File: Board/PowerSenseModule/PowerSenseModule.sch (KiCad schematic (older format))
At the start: 12 parts

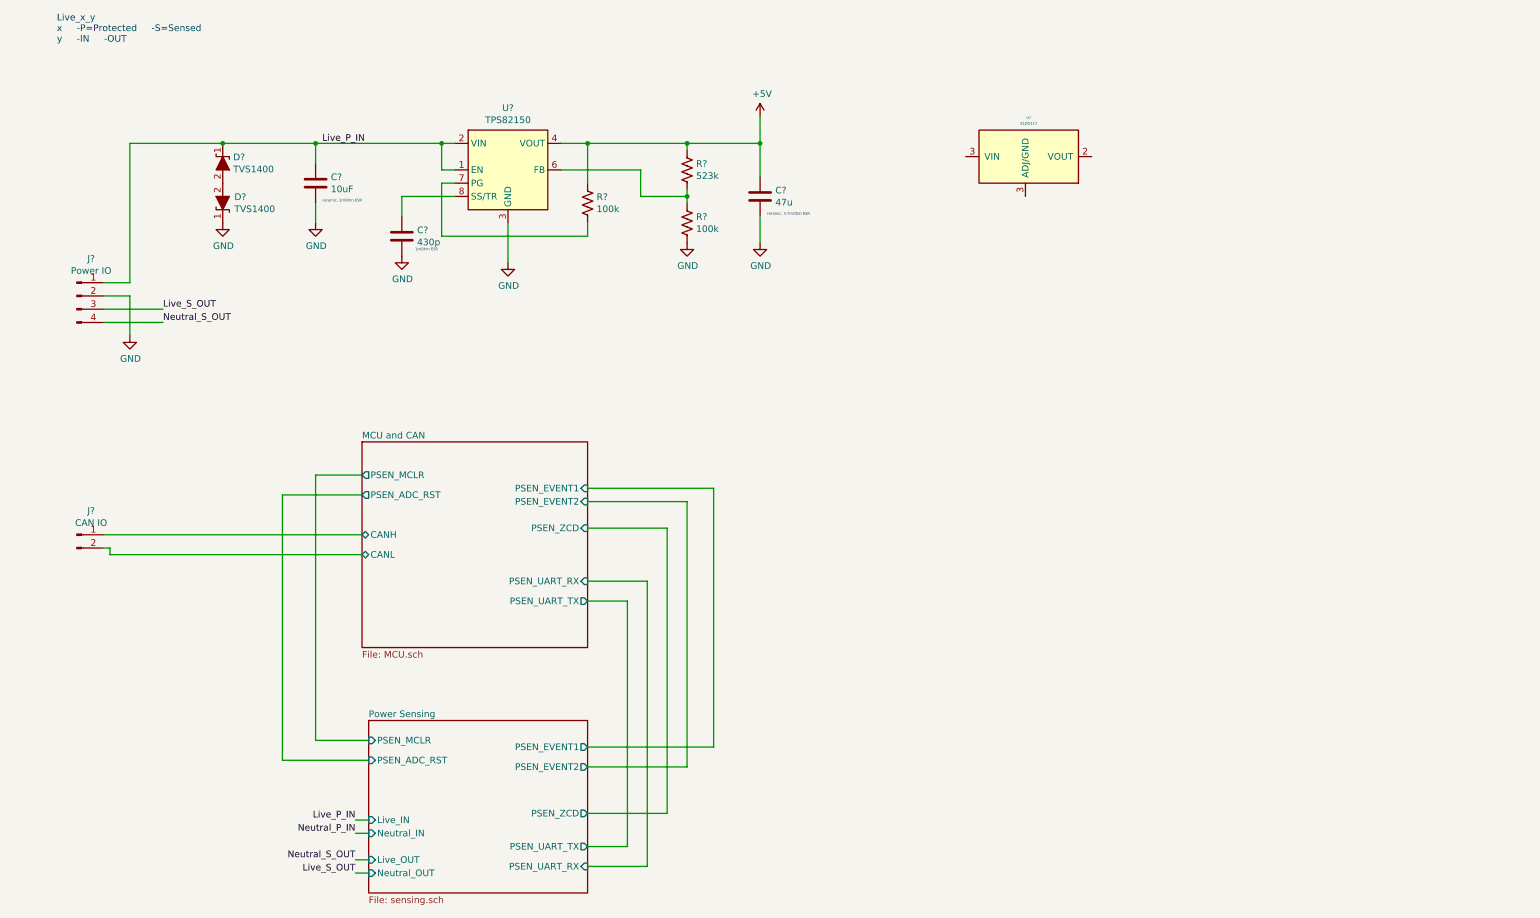
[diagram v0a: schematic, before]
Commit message: Added linear reg, cleaned up schematic
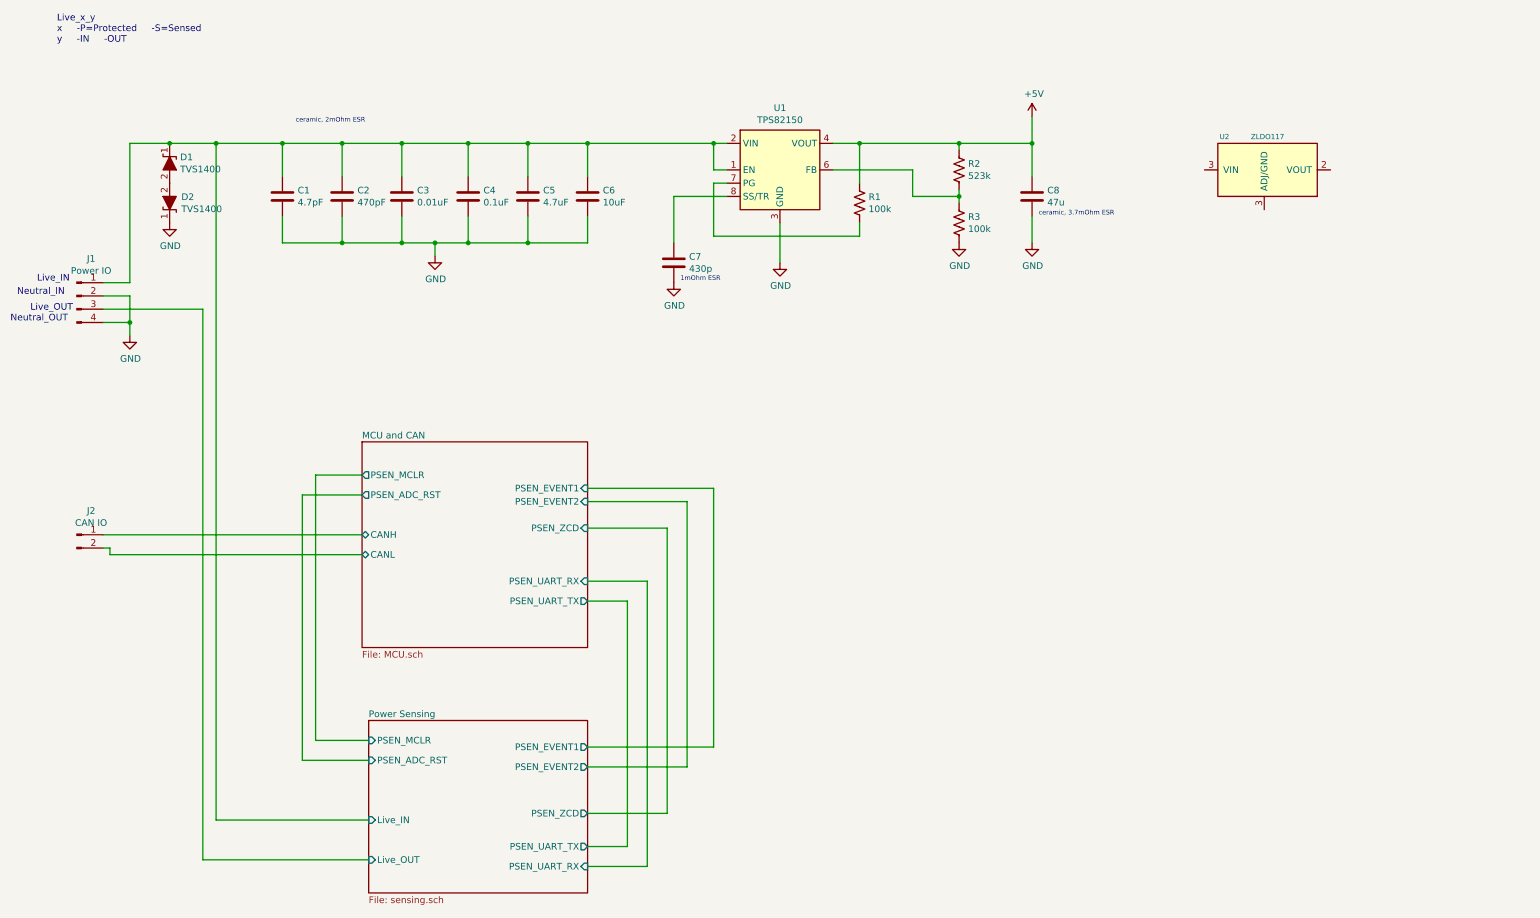
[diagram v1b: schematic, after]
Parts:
- added C1: 4.7pF, symbol Device:C
- added C2: 470pF, symbol Device:C
- added C3: 0.01uF, symbol Device:C
- added C4: 0.1uF, symbol Device:C
- added C5: 4.7uF, symbol Device:C
- gave numbers to parts that had none: 12
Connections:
- net Neutral_S_OUT is gone; now on net GND: J1.4 (Pin_4)
- net GND: now also C1.2, C2.2, C3.2, C4.2, C5.2
- net Live_P_IN renamed Power Sensing/Live_IN
- net Power Sensing/Live_IN: now also C1.1, C2.1, C3.1, C4.1, C5.1
- net Live_S_OUT renamed Power Sensing/Live_OUT
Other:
- note added: "Live_IN\n"
- note added: "Live_OUT\n\n"
- note added: "Neutral_IN\n"
- note added: "Neutral_OUT"
- moved on the sheet: C6, C7, C8, D1, D2, R1, R2, R3, U1, U2

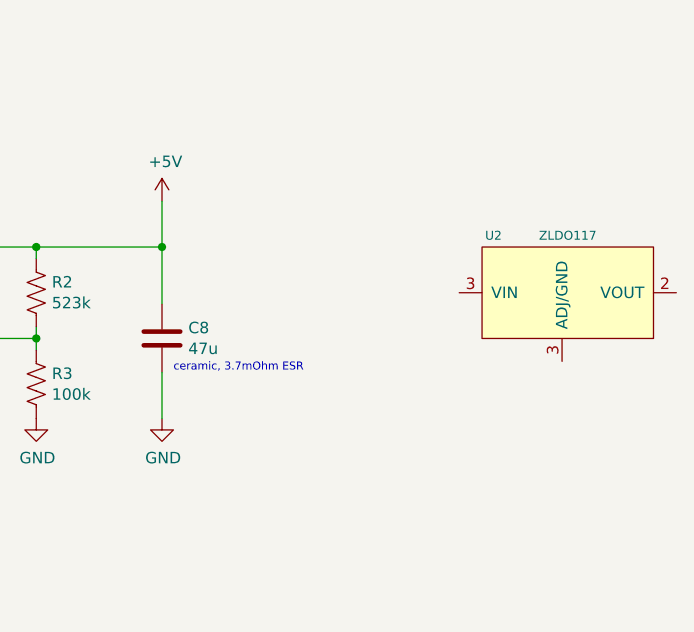
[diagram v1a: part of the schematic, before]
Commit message: Lin Reg Connected with cap, global power net, and wiring.
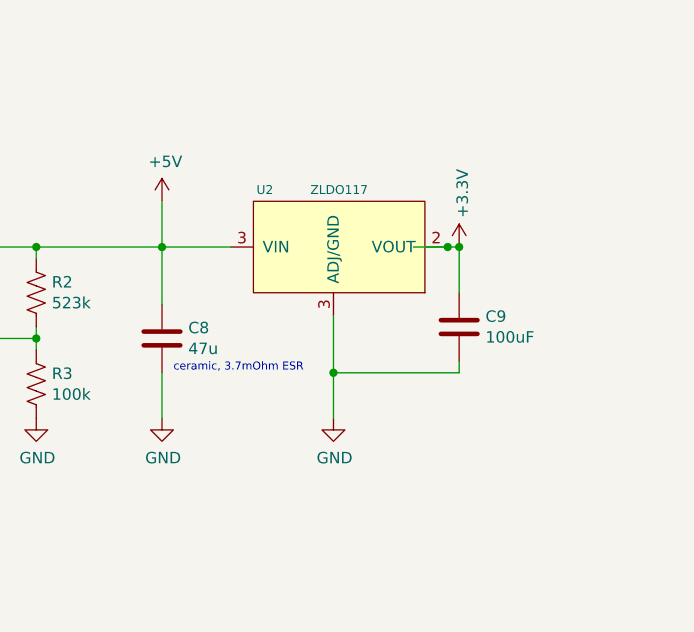
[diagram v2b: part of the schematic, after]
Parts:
- added C9: 100uF, symbol Device:C
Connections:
- net +5V: now also U2.3 (VIN)
- net GND: now also U2.3 (VIN), C9.2
- net +3V3: now reaches U2.2 (VOUT)
- net +3V3: now also C9.1
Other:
- moved on the sheet: U2
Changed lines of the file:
@@
 L F1_Power_ICs:ZLDO117 U2
 U 1 1 5D37AF29
-P 9950 1750
-F 0 "U2" H 9650 2000 39  0000 C CNN
-F 1 "ZLDO117" H 9975 2000 39  0000 C CNN
-F 2 "Package_TO_SOT_SMD:SOT-223" H 9800 2100 20  0001 C CNN
-F 3 "https://www.diodes.com/assets/Datasheets/ZLDO1117Q.pdf" H 9800 2100 20  0001 C CNN
-	1    9950 1750
+P 8950 1550
+F 0 "U2" H 8650 1800 39  0000 C CNN
+F 1 "ZLDO117" H 8975 1800 39  0000 C CNN
+F 2 "Package_TO_SOT_SMD:SOT-223" H 8800 1900 20  0001 C CNN
+F 3 "https://www.diodes.com/assets/Datasheets/ZLDO1117Q.pdf" H 8800 1900 20  0001 C CNN
+	1    8950 1550
 	1    0    0    -1
 $EndComp
@@
 Text Notes 500  2900 0    50   ~ 0
 Neutral_OUT
+$Comp
+L power:GND #PWR?
+U 1 1 5D33134A
+P 8950 2300
+F 0 "#PWR?" H 8950 2050 50  0001 C CNN
+F 1 "GND" H 8955 2127 50  0000 C CNN
+F 2 "" H 8950 2300 50  0001 C CNN
+F 3 "" H 8950 2300 50  0001 C CNN
+	1    8950 2300
+	1    0    0    -1
+$EndComp
+Wire Wire Line
+	8950 1850 8950 2100
+Wire Wire Line
+	8500 1550 8200 1550
+Wire Wire Line
+	9450 1550 9500 1550
+Connection ~ 8950 2100
+Wire Wire Line
+	8950 2100 8950 2300
+Wire Wire Line
+	9500 2100 8950 2100
+Connection ~ 9500 1550
+Wire Wire Line
+	9300 1550 9450 1550
+$Comp
+L Device:C C9
+U 1 1 5D39E84F
+P 9500 1900
+F 0 "C9" H 9615 1946 50  0000 L CNN
+F 1 "100uF" H 9615 1855 50  0000 L CNN
+F 2 "" H 9538 1750 50  0001 C CNN
+F 3 "~" H 9500 1900 50  0001 C CNN
+	1    9500 1900
+	1    0    0    -1
+$EndComp
+Wire Wire Line
+	9500 1550 9500 1750
+Wire Wire Line
+	9500 2050 9500 2100
+$Comp
+L power:+3.3V #PWR?
+U 1 1 5D3A49D9
+P 9500 1550
+F 0 "#PWR?" H 9500 1400 50  0001 C CNN
+F 1 "+3.3V" V 9515 1678 50  0000 L CNN
+F 2 "" H 9500 1550 50  0001 C CNN
+F 3 "" H 9500 1550 50  0001 C CNN
+	1    9500 1550
+	1    0    0    -1
+$EndComp
+Connection ~ 9450 1550
 $EndSCHEMATC

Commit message: Finalizing footprints - a
Changed footprints of 4.7u, 10u, 47u ceramic caps to 0805 from 0603.

Changed output cap of linear reg to 150u electrolytic 

Added tie net for grounds

Connector footprints

Added notes

TODO:
footprints of net tie, 150u electrolytic
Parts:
- removed C9: 100uF, symbol Device:C
- added C9: 150uF, symbol Device:CP
- added NT1: Net-Tie_3_Tee, symbol Device:Net-Tie_3_Tee
- C1, C2, C3, C4, C5, C7: footprint (none) -> Capacitor_SMD:C_0603_1608Metric_Pad1.05x0.95mm_HandSolder
- C6: footprint (none) -> Capacitor_SMD:C_0805_2012Metric_Pad1.15x1.40mm_HandSolder
- C8: value 47u -> 47uF; footprint (none) -> Capacitor_SMD:C_0805_2012Metric_Pad1.15x1.40mm_HandSolder
- J1: footprint (none) -> Connector_TE:DT13-4P
- J2: footprint (none) -> Connector_TE:DT13-2P
- R1, R2, R3: footprint (none) -> Resistor_SMD:R_0603_1608Metric_Pad1.05x0.95mm_HandSolder
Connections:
- net +3V3: now also C9.1
- net GND: now also C9.2, NT1.1
- new net GNDA: NT1.2
- new net GNDD: NT1.3
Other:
- note added: "Bypass capacitors need to be placed close to the IC and must be physically between the power and IC\n"
- note added: "Electrolytic low ESR"
- note added: "NOTES"
- note added: "Temp IC should be close to the power sensor\n"
- note added: "The TVS (zener) diodes need to be placed physically before the capacitors and before any connections to power sensor\n"
- note added: "The different grounds should only be connected at one junction using the net tie"
- note added: "The grounds should have their own planes and the power, digital, and analog sections should tried to be kept separate - different regions of the board"
- note removed: "Live_x_y\nx -P=Protected -S=Sensed\ny -IN -OUT"
- moved on the sheet: U2

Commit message: Finalizing Footprints PT B
Have two copies of everything, don't know why. Added NETI to remaining resistors and capacitor. Let's see
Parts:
- C9: footprint (none) -> Capacitor_SMD:C_Elec_8x10.2
- NT1: footprint (none) -> NetTie:NetTie-3_SMD_Pad2.0mm
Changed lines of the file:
@@
 F 0 "NT1" H 10750 981 50  0000 C CNN
 F 1 "Net-Tie_3_Tee" H 10750 890 50  0000 C CNN
-F 2 "" H 10750 800 50  0001 C CNN
+F 2 "NetTie:NetTie-3_SMD_Pad2.0mm" H 10750 800 50  0001 C CNN
 F 3 "~" H 10750 800 50  0001 C CNN
 	1    10750 800
@@
 F 0 "C9" H 10068 1946 50  0000 L CNN
 F 1 "150uF" H 10068 1855 50  0000 L CNN
-F 2 "" H 9988 1750 50  0001 C CNN
+F 2 "Capacitor_SMD:C_Elec_8x10.2" H 9988 1750 50  0001 C CNN
 F 3 "~" H 9950 1900 50  0001 C CNN
 	1    9950 1900

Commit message: Fixed footprint library paths
Changed TVS1400 clamp to project specific library and fixed library path for the microsip footprint
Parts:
- U1: footprint Package_LGA:Texas_MicroSiP-8-1EP_2.8x3.0mm_P0.65mm_EP1.1x1.9mm_SMD_ThermalVias -> Package_LGA:Texas_SIL0008D_MicroSiP-8-1EP_2.8x3mm_P0.65mm_EP1.1x1.9mm
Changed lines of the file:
@@
 F 0 "U1" H 6300 2217 50  0000 C CNN
 F 1 "TPS82150" H 6300 2126 50  0000 C CNN
-F 2 "Package_LGA:Texas_MicroSiP-8-1EP_2.8x3.0mm_P0.65mm_EP1.1x1.9mm_SMD_ThermalVias" H 6300 1100 50  0001 C CNN
+F 2 "Package_LGA:Texas_SIL0008D_MicroSiP-8-1EP_2.8x3mm_P0.65mm_EP1.1x1.9mm" H 6300 1100 50  0001 C CNN
 F 3 "http://www.ti.com/lit/ds/symlink/tps82150.pdf" H 6300 1000 50  0001 C CNN
 	1    6300 1750

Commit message: PCB Design Began. Design Changes are incoming though.
PCB placement began, changes to schematic will be made. Reference google docs for said changes along with date.
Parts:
- C6: footprint Capacitor_SMD:C_0805_2012Metric_Pad1.15x1.40mm_HandSolder -> Capacitor_SMD:CP_Elec_4x5.8
- C7: value 430p -> 470p
- C8: footprint Capacitor_SMD:C_0805_2012Metric_Pad1.15x1.40mm_HandSolder -> Capacitor_SMD:CP_Elec_6.3x5.8
- C9: value 150uF -> 100uF; footprint Capacitor_SMD:C_Elec_8x10.2 -> Capacitor_SMD:CP_Elec_6.3x5.9
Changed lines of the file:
@@
 F 0 "C6" H 4965 1996 50  0000 L CNN
 F 1 "10uF" H 4965 1905 50  0000 L CNN
-F 2 "Capacitor_SMD:C_0805_2012Metric_Pad1.15x1.40mm_HandSolder" H 4888 1800 50  0001 C CNN
+F 2 "Capacitor_SMD:CP_Elec_4x5.8" H 4888 1800 50  0001 C CNN
 F 3 "~" H 4850 1950 50  0001 C CNN
 	1    4850 1950
@@
 P 5500 2450
 F 0 "C7" H 5615 2496 50  0000 L CNN
-F 1 "430p" H 5615 2405 50  0000 L CNN
+F 1 "470p" H 5615 2405 50  0000 L CNN
 F 2 "Capacitor_SMD:C_0603_1608Metric_Pad1.05x0.95mm_HandSolder" H 5538 2300 50  0001 C CNN
 F 3 "~" H 5500 2450 50  0001 C CNN
@@
 F 0 "C8" H 8315 1996 50  0000 L CNN
 F 1 "47uF" H 8315 1905 50  0000 L CNN
-F 2 "Capacitor_SMD:C_0805_2012Metric_Pad1.15x1.40mm_HandSolder" H 8238 1800 50  0001 C CNN
+F 2 "Capacitor_SMD:CP_Elec_6.3x5.8" H 8238 1800 50  0001 C CNN
 F 3 "~" H 8200 1950 50  0001 C CNN
 	1    8200 1950
@@
 P 9950 1900
 F 0 "C9" H 10068 1946 50  0000 L CNN
-F 1 "150uF" H 10068 1855 50  0000 L CNN
-F 2 "Capacitor_SMD:C_Elec_8x10.2" H 9988 1750 50  0001 C CNN
+F 1 "100uF" H 10068 1855 50  0000 L CNN
+F 2 "Capacitor_SMD:CP_Elec_6.3x5.9" H 9988 1750 50  0001 C CNN
 F 3 "~" H 9950 1900 50  0001 C CNN
 	1    9950 1900

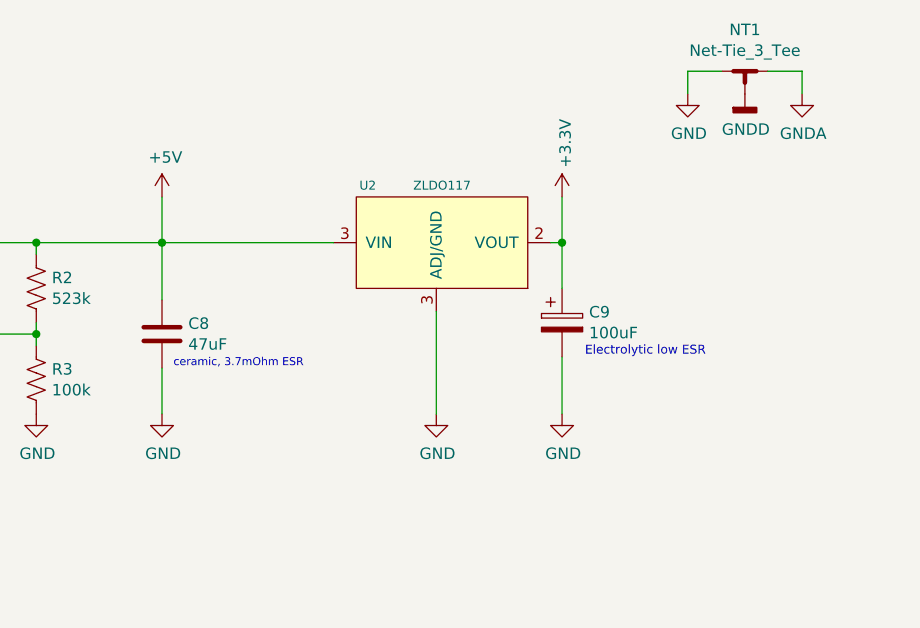
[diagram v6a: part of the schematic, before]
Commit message: Started design change
Changing MCU to 5V dspic33ev32gm102
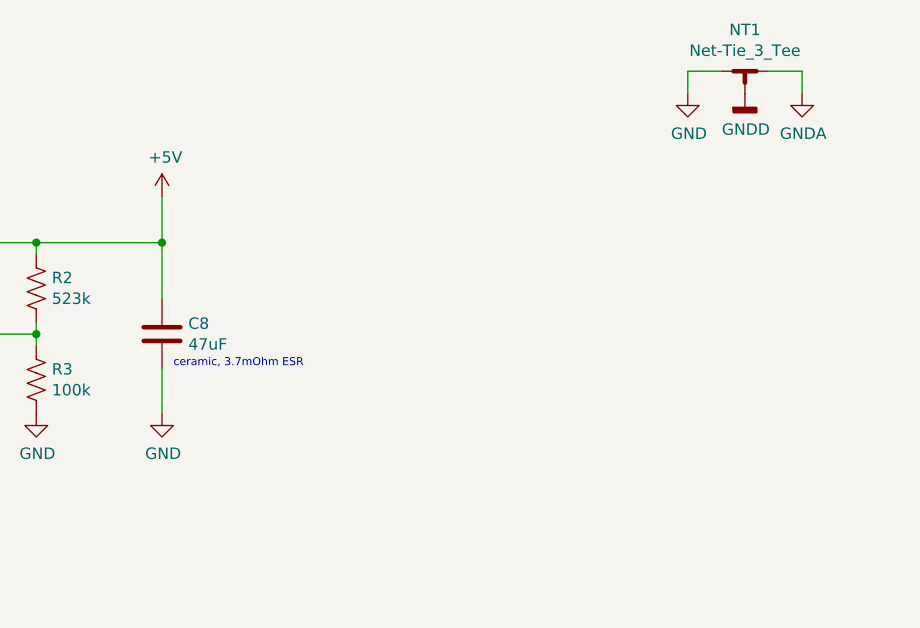
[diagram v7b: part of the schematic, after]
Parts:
- removed C9: 100uF, Capacitor_SMD:CP_Elec_6.3x5.9, symbol Device:CP
- removed U2: ZLDO117, Package_TO_SOT_SMD:SOT-223, symbol F1_Power_ICs:ZLDO117
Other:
- note removed: "Electrolytic low ESR"
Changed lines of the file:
@@
 Text Notes 6400 6050 0    39   ~ 0
 Temp IC should be close to the power sensor\n
-Wire Wire Line
-	9950 1350 9950 1550
-$Comp
-L power:+3.3V #PWR010
-U 1 1 5D3A49D9
-P 9950 1350
-F 0 "#PWR010" H 9950 1200 50  0001 C CNN
-F 1 "+3.3V" V 9965 1478 50  0000 L CNN
-F 2 "" H 9950 1350 50  0001 C CNN
-F 3 "" H 9950 1350 50  0001 C CNN
-	1    9950 1350
-	1    0    0    -1
-$EndComp
-Wire Wire Line
-	9950 1550 9950 1750
-Connection ~ 9950 1550
-Wire Wire Line
-	9900 1550 9950 1550
-$Comp
-L power:GND #PWR09
-U 1 1 5D33134A
-P 9400 2300
-F 0 "#PWR09" H 9400 2050 50  0001 C CNN
-F 1 "GND" H 9405 2127 50  0000 C CNN
-F 2 "" H 9400 2300 50  0001 C CNN
-F 3 "" H 9400 2300 50  0001 C CNN
-	1    9400 2300
-	1    0    0    -1
-$EndComp
 Text Notes 8250 2100 0    35   ~ 0
 ceramic, 3.7mOhm ESR\n
-$Comp
-L F1_Power_ICs:ZLDO117 U2
-U 1 1 5D37AF29
-P 9400 1550
-F 0 "U2" H 9100 1800 39  0000 C CNN
-F 1 "ZLDO117" H 9425 1800 39  0000 C CNN
-F 2 "Package_TO_SOT_SMD:SOT-223" H 9250 1900 20  0001 C CNN
-F 3 "https://www.diodes.com/assets/Datasheets/ZLDO1117Q.pdf" H 9250 1900 20  0001 C CNN
-	1    9400 1550
-	1    0    0    -1
-$EndComp
-Wire Wire Line
-	9400 1850 9400 2300
-$Comp
-L Device:CP C9
-U 1 1 5D424F64
-P 9950 1900
-F 0 "C9" H 10068 1946 50  0000 L CNN
-F 1 "100uF" H 10068 1855 50  0000 L CNN
-F 2 "Capacitor_SMD:CP_Elec_6.3x5.9" H 9988 1750 50  0001 C CNN
-F 3 "~" H 9950 1900 50  0001 C CNN
-	1    9950 1900
-	1    0    0    -1
-$EndComp
-$Comp
-L power:GND #PWR011
-U 1 1 5D425C0E
-P 9950 2300
-F 0 "#PWR011" H 9950 2050 50  0001 C CNN
-F 1 "GND" H 9955 2127 50  0000 C CNN
-F 2 "" H 9950 2300 50  0001 C CNN
-F 3 "" H 9950 2300 50  0001 C CNN
-	1    9950 2300
-	1    0    0    -1
-$EndComp
-Wire Wire Line
-	9950 2300 9950 2050
-Text Notes 10050 2050 0    39   ~ 0
-Electrolytic low ESR
-Wire Wire Line
-	8200 1550 8950 1550
 $EndSCHEMATC
